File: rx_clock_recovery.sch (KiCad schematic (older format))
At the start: 21 parts, among them U1 4029, U10 LM339, U11 74HC14, U2 27C128, U3 4029, U8 74HC161, U9 ZN429E-8

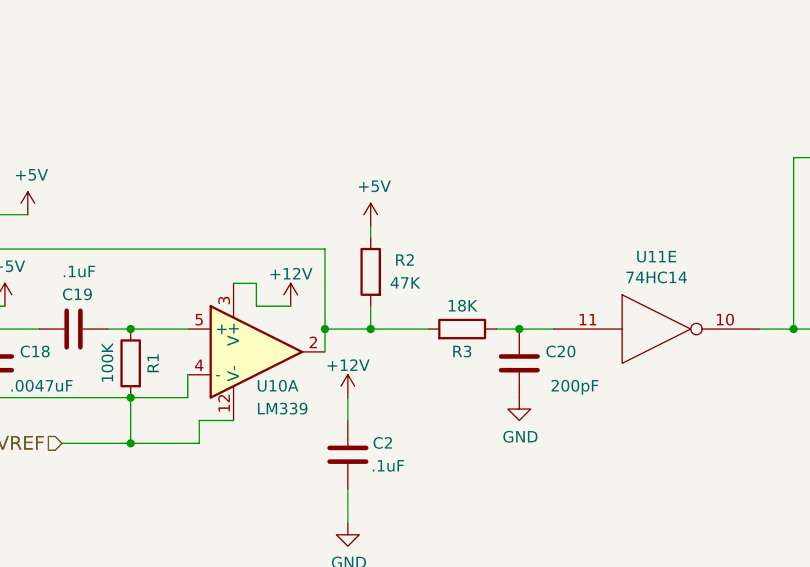
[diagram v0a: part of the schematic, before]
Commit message: Corrected transcription errors.
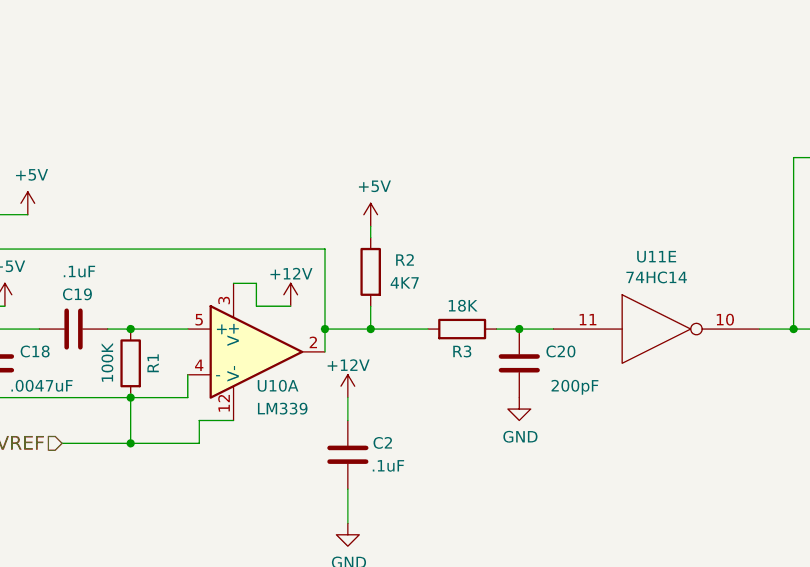
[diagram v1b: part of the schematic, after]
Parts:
- R2: value 47K -> 4K7
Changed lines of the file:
@@
 P 7600 5000
 F 0 "R2" H 7450 5050 50  0000 C CNN
-F 1 "47K" H 7450 4950 50  0000 C CNN
+F 1 "4K7" H 7450 4950 50  0000 C CNN
 F 2 "Resistors_THT:R_Axial_DIN0204_L3.6mm_D1.6mm_P7.62mm_Horizontal" V 7530 5000 50  0001 C CNN
 F 3 "" H 7600 5000 50  0001 C CNN
